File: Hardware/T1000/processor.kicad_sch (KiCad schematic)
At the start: 32 parts, among them J6 SOICbite, Q1 IRLML0060TRPBF, U2 RP2040, U3 W25Q128JVS, Y1 445I23D12M00000

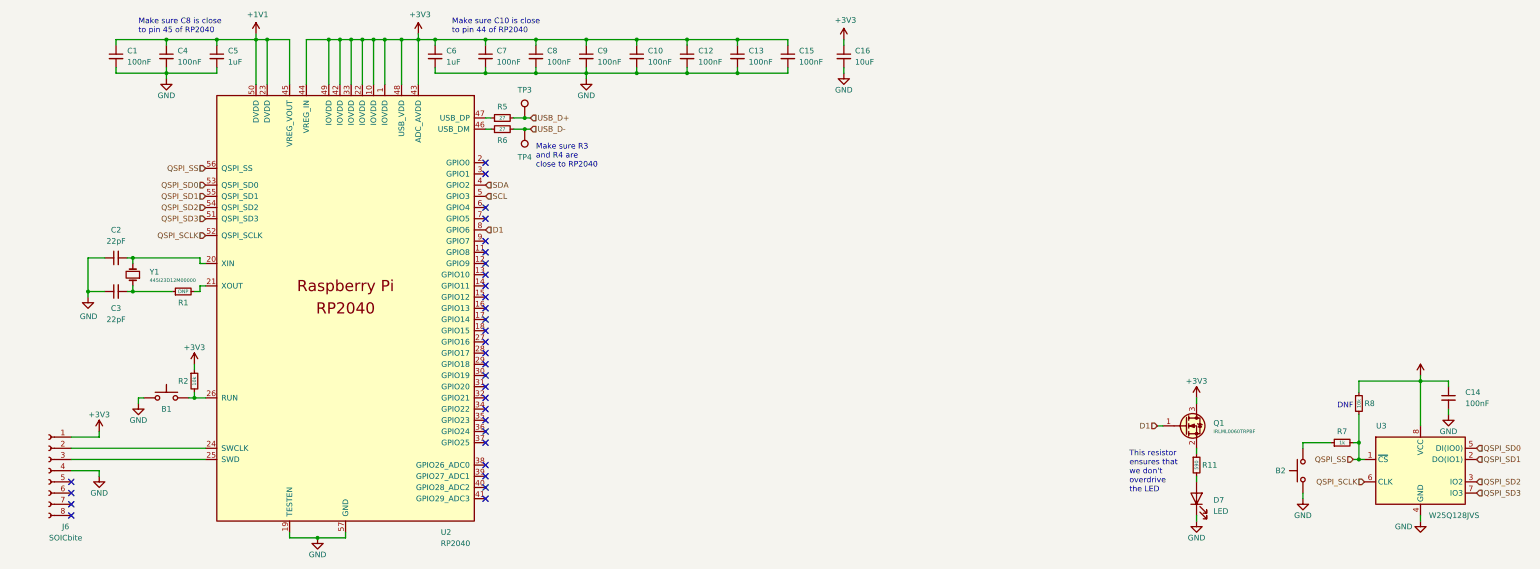
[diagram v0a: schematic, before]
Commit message: added SD card
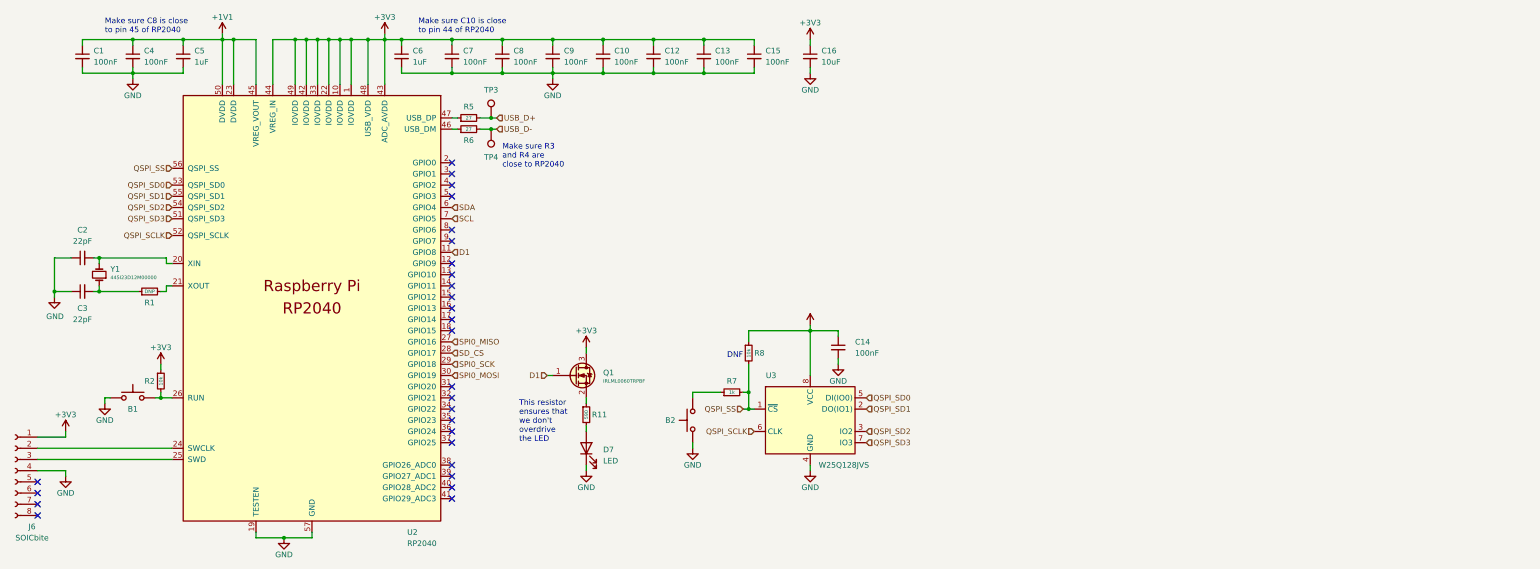
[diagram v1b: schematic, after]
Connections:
- net D1: now also U2.11 (GPIO8); no longer U2.8 (GPIO6)
- net SCL: now also U2.7 (GPIO5); no longer U2.5 (GPIO3)
- net SDA: now also U2.6 (GPIO4); no longer U2.4 (GPIO2)
- net SPI0_MISO: now reaches U2.27 (GPIO16)
- net SD_CS: now reaches U2.28 (GPIO17)
- net SPI0_SCK: now reaches U2.29 (GPIO18)
- net SPI0_MOSI: now reaches U2.30 (GPIO19)
- no-connect marks 31 -> 27
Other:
- moved on the sheet: B1, B2, C1, C10, C12, C13, C14, C15, C16, C2, C3, C4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
